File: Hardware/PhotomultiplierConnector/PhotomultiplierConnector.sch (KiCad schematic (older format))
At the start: 25 parts

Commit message: split (previousle one) pcb project to three separate pcbs
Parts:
- removed EL1: Photomultiplier, GammaSpectrometer:PhotomultiplierGeneric, symbol GammaSpectrometer:Photomultiplier
- added EL1: Photomultiplier, PhotomultiplierConnector:PhotomultiplierGeneric, symbol PhotomultiplierConnector:Photomultiplier
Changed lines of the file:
@@
 $Descr A4 11693 8268
 encoding utf-8
-Sheet 4 7
+Sheet 1 1
 Title ""
 Date ""
@@
 Text GLabel 1450 6600 0    50   Input ~ 0
 ANODE_OUTPUT
-$Comp
-L GammaSpectrometer:Photomultiplier EL1
-U 1 1 5EE61F2A
-P 6350 4050
-F 0 "EL1" H 6425 4365 50  0000 C CNN
-F 1 "Photomultiplier" H 6425 4274 50  0000 C CNN
-F 2 "GammaSpectrometer:PhotomultiplierGeneric" H 6350 4300 50  0001 C CNN
-F 3 "" H 6350 4300 50  0001 C CNN
-	1    6350 4050
-	0    1    1    0
-$EndComp
 Wire Wire Line
 	5750 1650 5750 3450
@@
 AR Path="/5EFA52FA/5EE7139E" Ref="D?"  Part="1"
 AR Path="/5EDA585D/5EE7139E" Ref="D11"  Part="1"
+AR Path="/5EE7139E" Ref="D11"  Part="1"
 F 0 "D11" H 1650 7166 50  0000 C CNN
 F 1 "1n148" H 1650 7075 50  0000 C CNN
@@
 AR Path="/5EFA52FA/5EE713AA" Ref="#PWR?"  Part="1"
 AR Path="/5EDA585D/5EE713AA" Ref="#PWR02"  Part="1"
+AR Path="/5EE713AA" Ref="#PWR02"  Part="1"
 F 0 "#PWR02" H 1650 6950 50  0001 C CNN
 F 1 "GND" H 1655 7027 50  0000 C CNN
@@
 Text Notes 2050 2000 0    50   ~ 0
 todo fix later
+$Comp
+L PhotomultiplierConnector:Photomultiplier EL1
+U 1 1 5FA1B808
+P 6350 4050
+F 0 "EL1" V 6379 4228 50  0000 L CNN
+F 1 "Photomultiplier" V 6470 4228 50  0000 L CNN
+F 2 "PhotomultiplierConnector:PhotomultiplierGeneric" H 6350 4300 50  0001 C CNN
+F 3 "" H 6350 4300 50  0001 C CNN
+	1    6350 4050
+	0    1    1    0
+$EndComp
 $EndSCHEMATC

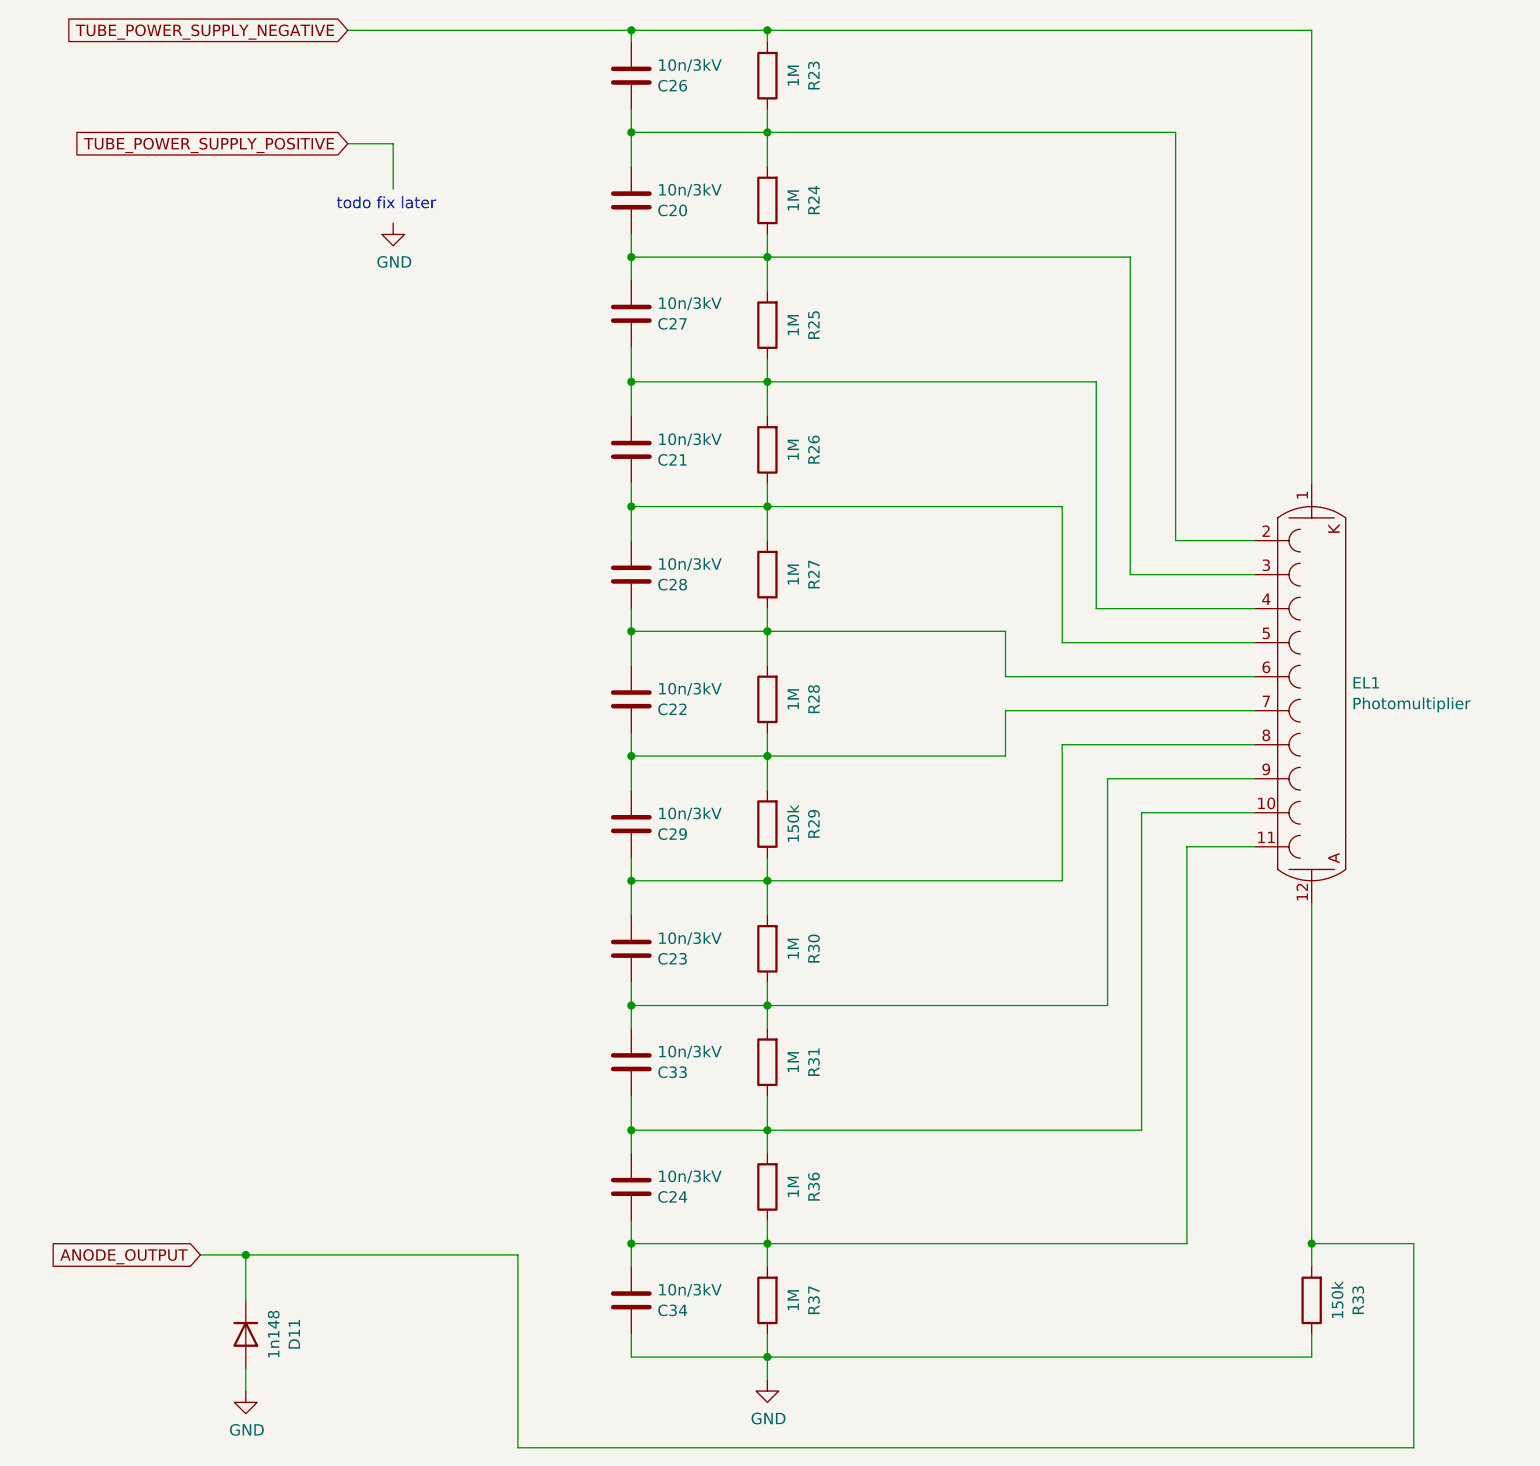
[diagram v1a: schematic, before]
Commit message: finished circuit for tube polarization, in script for polar placements added PoC of generating pcb outlines using arcs and lines
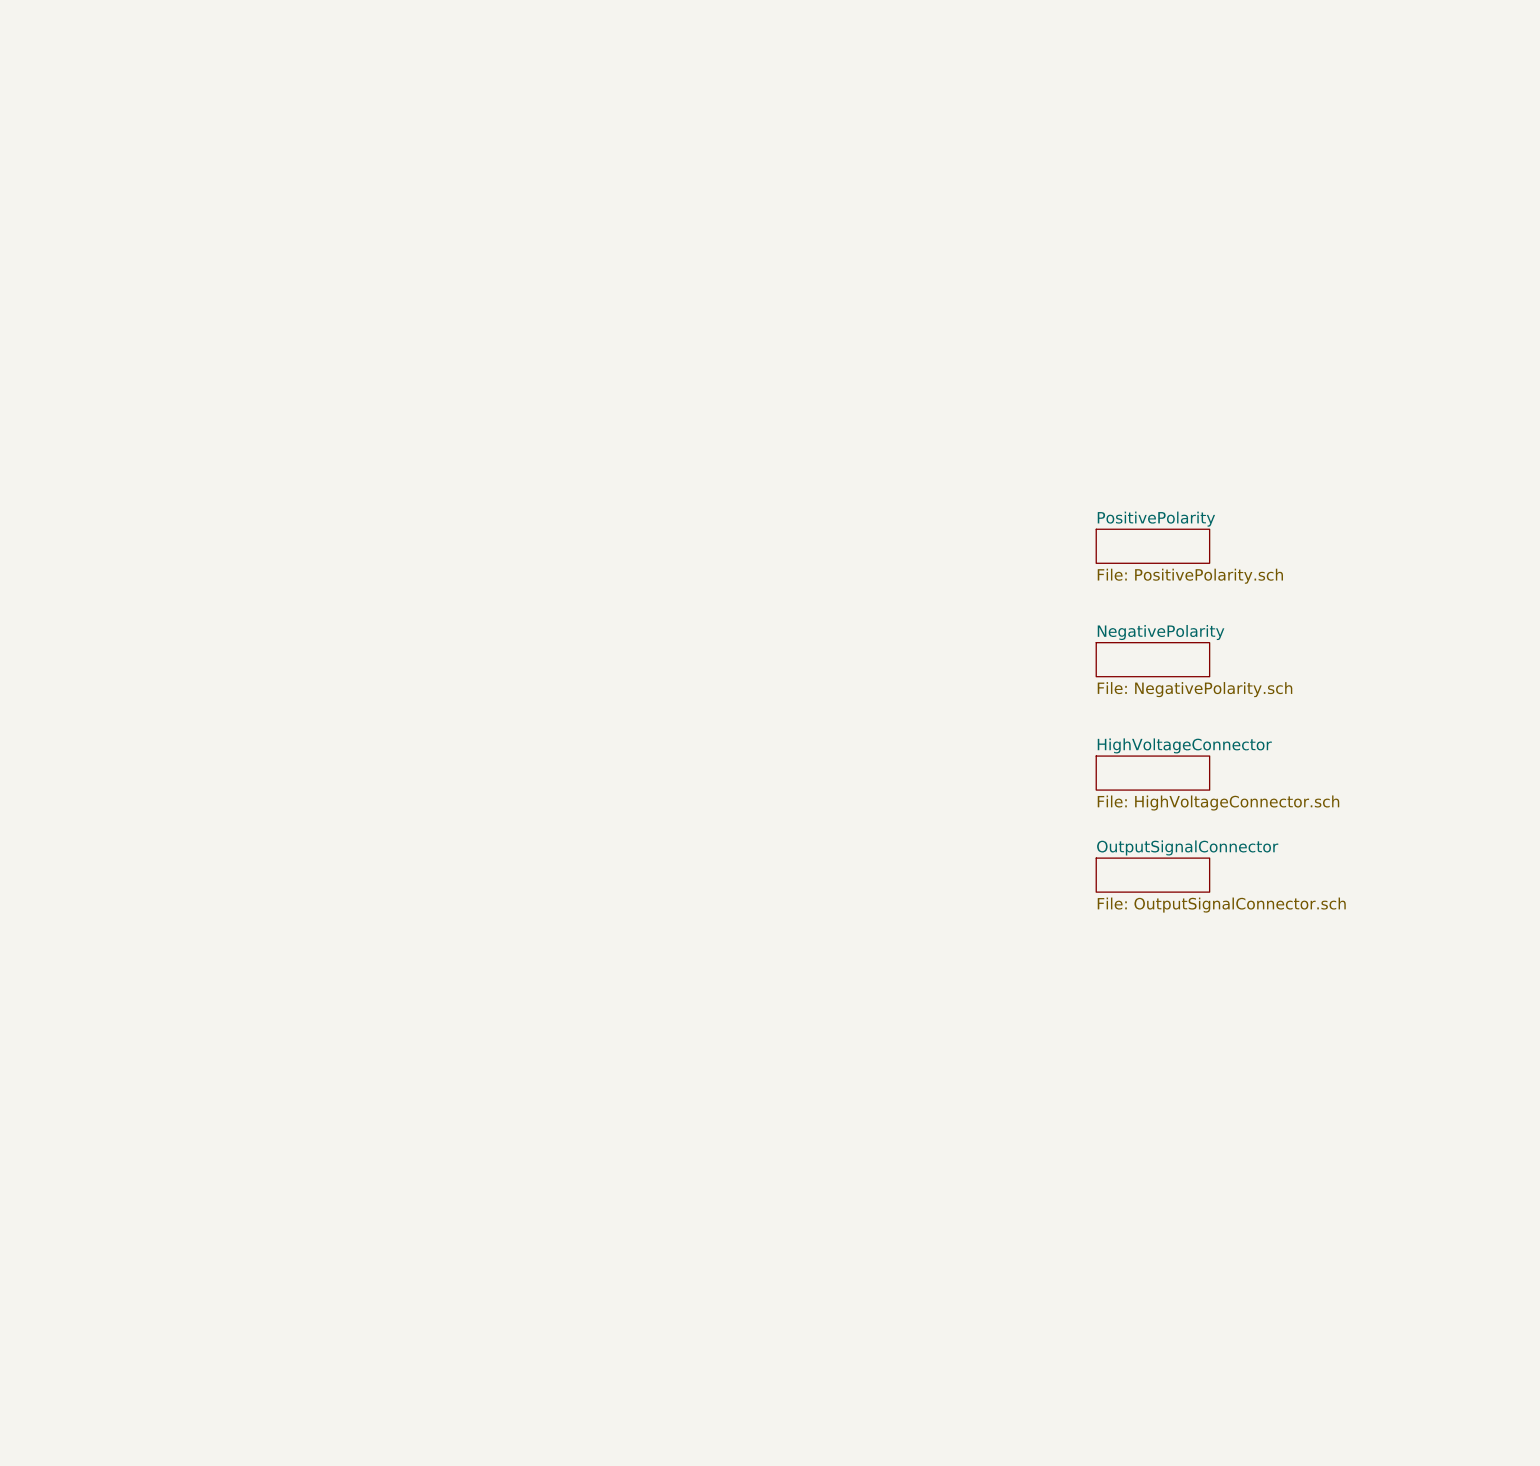
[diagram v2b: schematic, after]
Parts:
- removed C20, C21, C22, C23, C24, C26, C27, C28, C29, C33, C34: 10n/3kV, Capacitor_SMD:C_1210_3225Metric, symbol Device:C
- removed D11: 1n148, Diode_SMD:D_MELF, symbol Device:D
- removed EL1: Photomultiplier, PhotomultiplierConnector:PhotomultiplierGeneric, symbol PhotomultiplierConnector:Photomultiplier
- removed R23, R24, R25, R26, R27, R28, R30, R31, R36, R37: 1M, Resistor_SMD:R_MELF_MMB-0207, symbol Device:R
- removed R29, R33: 150k, Resistor_SMD:R_MELF_MMB-0207, symbol Device:R
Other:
- note removed: "todo fix later"

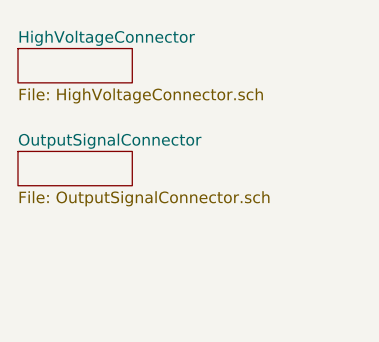
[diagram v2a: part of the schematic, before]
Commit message: finished script for automatic component placement - it was overengineering, abandonend ide aof a circular pcb for photomultiplier connector
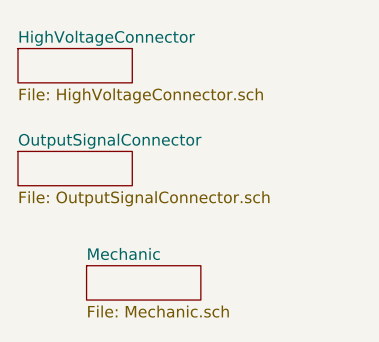
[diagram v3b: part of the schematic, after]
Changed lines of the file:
@@
 $Descr A4 11693 8268
 encoding utf-8
-Sheet 1 5
+Sheet 1 6
 Title ""
 Date ""
@@
 F1 "OutputSignalConnector.sch" 50
 $EndSheet
+$Sheet
+S 5700 5350 500  150
+U 5FA43545
+F0 "Mechanic" 50
+F1 "Mechanic.sch" 50
+$EndSheet
 $EndSCHEMATC
